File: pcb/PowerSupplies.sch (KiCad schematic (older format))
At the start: 23 parts, among them Q12 ZXTP25020DGTA, U13 TL431BQDBZR, U2 LM2941S, U3 LM2937EM-5.0

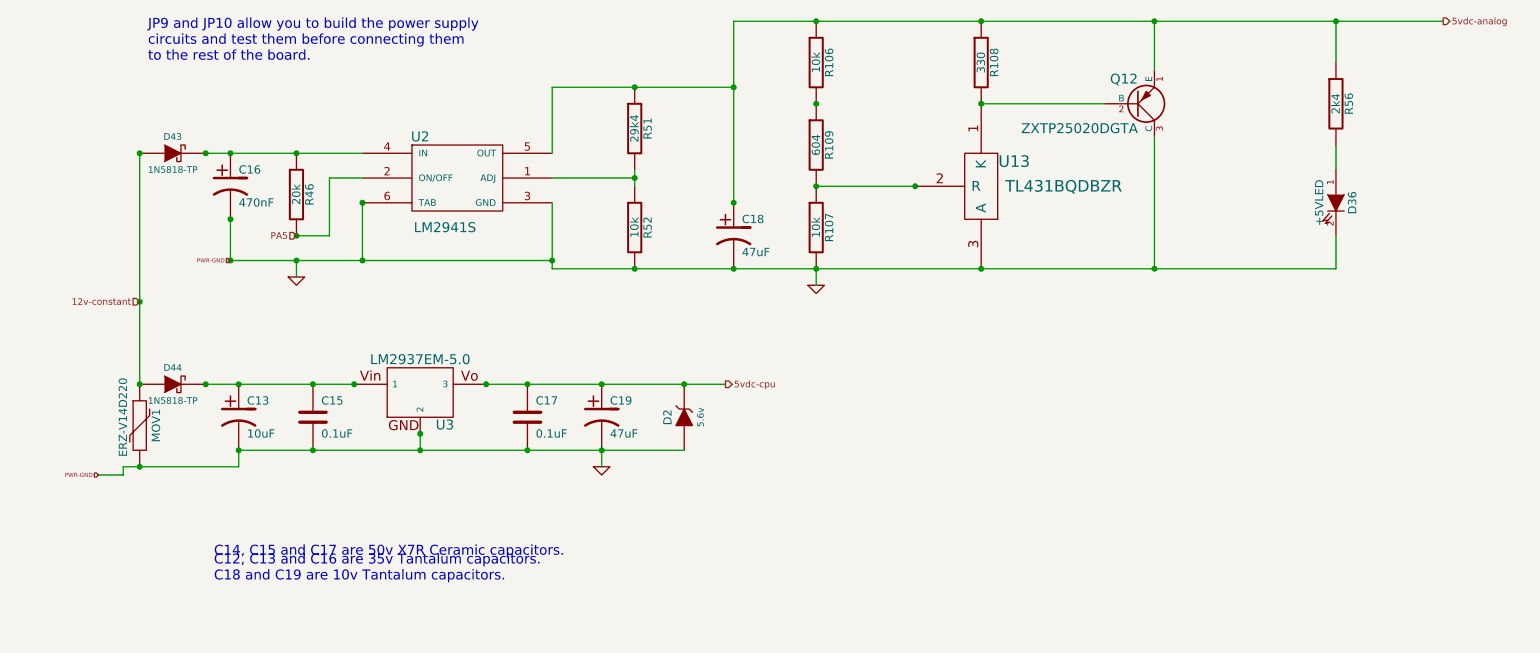
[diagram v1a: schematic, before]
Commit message: schematics update
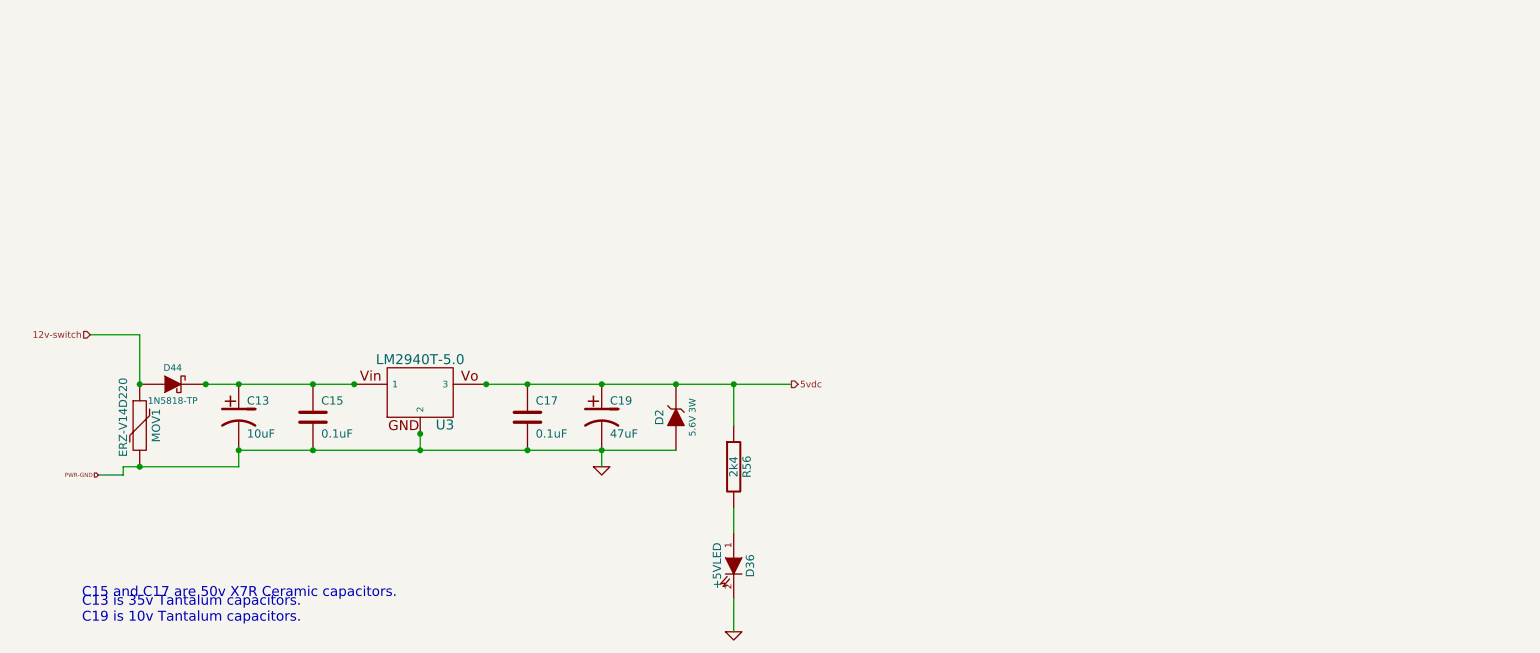
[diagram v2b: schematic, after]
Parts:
- removed C16: 470nF, symbol CP1
- removed C18: 47uF, symbol CP1
- removed D43: 1N5818-TP, symbol DIODESCH
- removed Q12: ZXTP25020DGTA, symbol PNP
- removed R106, R107, R52: 10k, symbol R
- removed R108: 330, symbol R
- removed R109: 604, symbol R
- removed R46: 20k, symbol R
- removed R51: 29k4, symbol R
- removed U13: TL431BQDBZR, symbol TL431LP
- removed U2: LM2941S, symbol LM2941S
- D2: value 5.6v -> 5.6V 3W; footprint (none) -> ~
- U3: value LM2937EM-5.0 -> LM2940T-5.0
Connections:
- net 5vdc-cpu is gone; now on net 5vdc: C17.1, C19.1, D2.2 (K), U3.3
- net 12v-constant renamed 12v-switch
- net 5vdc-analog renamed 5vdc
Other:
- note added: "C13 is 35v Tantalum capacitors.\nC19 is 10v Tantalum capacitors."
- note added: "C15 and C17 are 50v X7R Ceramic capacitors."
- note removed: "C12, C13 and C16 are 35v Tantalum capacitors.\nC18 and C19 are 10v Tantalum capacitors."
- note removed: "C14, C15 and C17 are 50v X7R Ceramic capacitors."
- note removed: "JP9 and JP10 allow you to build the power supply\ncircuits and test them before connecting them\nto the rest of the board."
- moved on the sheet: D36, R56
